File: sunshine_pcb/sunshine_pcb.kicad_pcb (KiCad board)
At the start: 4 copper layers, 42 x 52 mm, 54 parts, among them J1 Soldered, J2 Conn_01x03, J3 Soldered, J5 VerticalUSB, Q1 AO3400A, SW1 Fingertech, U1 ESP32-S3-WROOM-1, U2 SPX1117M3, U3 LIS3MDL, U4 ADXL375, U8 USBLC6-2P6

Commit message: Update PCB
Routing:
- added copper zone on In1.Cu, net /BATT1_+
- added copper zone on In2.Cu, net GND
- added copper zone on In1.Cu, net VDC
- removed copper zone on In2.Cu, net /BATT1_+
- removed copper zone on In1.Cu, net GND
- removed copper zone on In2.Cu, net VDC
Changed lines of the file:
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@@
 	)
 	(segment
+		(start 104.5 118.25)
+		(end 103 116.75)
+		(width 0.25)
+		(layer "F.Cu")
+		(net 20)
+	)
+	(segment
+		(start 103 116.75)
+		(end 102.41 116.75)
+		(width 0.25)
+		(layer "F.Cu")
+		(net 20)
+	)
+	(segment
 		(start 96.224 114.538588)
 		(end 98.511412 116.826)
@@
 	)
 	(segment
+		(start 103.468784 116.75)
+		(end 104.073 116.145784)
+		(width 0.25)
+		(layer "B.Cu")
+		(net 20)
+	)
+	(segment
 		(start 112.151 107.349)
 		(end 113.5 106)
@@
 	)
 	(segment
-		(start 102.425 116.75)
-		(end 103.222711 116.75)
-		(width 0.25)
-		(layer "B.Cu")
-		(net 20)
-	)
-	(segment
 		(start 96 133)
 		(end 96 131.1)
@@
 	)
 	(segment
-		(start 102.425 116.75)
-		(end 102.41 116.75)
-		(width 0.25)
-		(layer "B.Cu")
-		(net 20)
-	)
-	(segment
 		(start 96 109)
 		(end 96.75 109.75)
@@
 	)
 	(segment
-		(start 104.073 115.899711)
-		(end 104.073 115.637912)
-		(width 0.25)
-		(layer "B.Cu")
-		(net 20)
-	)
-	(segment
 		(start 107 115.5)
 		(end 108 115.5)
@@
 	)
 	(segment
-		(start 103.222711 116.75)
-		(end 104.073 115.899711)
-		(width 0.25)
-		(layer "B.Cu")
-		(net 20)
-	)
-	(segment
 		(start 108.75 115.5)
 		(end 112.589561 115.5)
@@
 	)
 	(segment
+		(start 102.41 116.75)
+		(end 103.468784 116.75)
+		(width 0.25)
+		(layer "B.Cu")
+		(net 20)
+	)
+	(segment
 		(start 99.613708 133.428)
 		(end 102.786293 133.428)
@@
 	)
 	(segment
+		(start 104.073 116.145784)
+		(end 104.073 115.637912)
+		(width 0.25)
+		(layer "B.Cu")
+		(net 20)
+	)
+	(segment
 		(start 103.25 110.75)
 		(end 102.5 110)
@@
 	)
 	(segment
-		(start 104.5 118.25)
-		(end 103.91 118.25)
-		(width 0.25)
-		(layer "In2.Cu")
-		(net 20)
-	)
-	(segment
-		(start 103.91 118.25)
-		(end 102.41 116.75)
-		(width 0.25)
-		(layer "In2.Cu")
-		(net 20)
-	)
-	(segment
 		(start 106 115.5)
 		(end 106.5 116)
@@
 	)
 	(segment
-		(start 102.454422 105.765833)
-		(end 103.970255 104.25)
-		(width 0.25)
-		(layer "In2.Cu")
-		(net 28)
-	)
-	(segment
-		(start 101.885412 105.674)
-		(end 102.362588 105.674)
+		(start 102.376026 105.65)
+		(end 100.823973 105.65)
 		(width 0.25)
-		(layer "In2.Cu")
+		(layer "In1.Cu")
 		(net 28)
 	)
 	(segment
-		(start 102.362588 105.674)
-		(end 102.454422 105.765833)
+		(start 104.25 104.25)
+		(end 103.776026 104.25)
 		(width 0.25)
-		(layer "In2.Cu")
+		(layer "In1.Cu")
 		(net 28)
 	)
 	(segment
-		(start 100.204559 106.269414)
+		(start 100.823973 105.65)
 		(end 98.602572 107.871401)
 		(width 0.25)
-		(layer "In2.Cu")
-		(net 28)
-	)
-	(segment
-		(start 103.970255 104.25)
-		(end 104.25 104.25)
-		(width 0.25)
-		(layer "In2.Cu")
-		(net 28)
-	)
-	(segment
-		(start 101.548 106.011412)
-		(end 101.885412 105.674)
-		(width 0.25)
-		(layer "In2.Cu")
-		(net 28)
-	)
-	(segment
-		(start 101.548 106.269414)
-		(end 100.204559 106.269414)
-		(width 0.25)
-		(layer "In2.Cu")
+		(layer "In1.Cu")
 		(net 28)
 	)
 	(segment
-		(start 101.548 106.269414)
-		(end 101.548 106.011412)
+		(start 103.776026 104.25)
+		(end 102.376026 105.65)
 		(width 0.25)
-		(layer "In2.Cu")
+		(layer "In1.Cu")
 		(net 28)
 	)
@@
 	)
 	(segment
-		(start 104.474 116.276)
-		(end 102.5 118.25)
+		(start 105.002983 108.758949)
+		(end 104.474 109.287932)
 		(width 0.15)
 		(layer "B.Cu")
@@
 	)
 	(segment
-		(start 102.5 118.25)
+		(start 103 118.25)
 		(end 96.17 118.25)
 		(width 0.15)
@@
 	)
 	(segment
-		(start 105.002983 108.758949)
-		(end 104.474 109.287932)
+		(start 104.474 109.287932)
+		(end 104.474 116.776)
 		(width 0.15)
 		(layer "B.Cu")
@@
 	)
 	(segment
-		(start 104.474 109.287932)
-		(end 104.474 116.276)
+		(start 104.474 116.776)
+		(end 103 118.25)
 		(width 0.15)
 		(layer "B.Cu")
@@
 	)
 	(segment
-		(start 103 115.5)
-		(end 103 118.25)
+		(start 103 116.1829)
+		(end 104.4571 117.64)
 		(width 0.15)
 		(layer "F.Cu")
@@
 	)
 	(segment
-		(start 103 118.25)
+		(start 104.72 117.64)
+		(end 105.18 118.1)
+		(width 0.15)
+		(layer "F.Cu")
+		(net 63)
+	)
+	(segment
+		(start 104.4571 117.64)
+		(end 104.72 117.64)
+		(width 0.15)
+		(layer "F.Cu")
+		(net 63)
+	)
+	(segment
+		(start 105.18 118.1)
+		(end 105.18 120.43)
+		(width 0.15)
+		(layer "F.Cu")
+		(net 63)
+	)
+	(segment
+		(start 105.18 120.43)
 		(end 107.6 122.85)
 		(width 0.15)
@@
 	)
 	(segment
+		(start 103 115.5)
+		(end 103 116.1829)
+		(width 0.15)
+		(layer "F.Cu")
+		(net 63)
+	)
+	(segment
 		(start 107.6 122.85)
 		(end 107.6 128.25)
@@
 	)
 	(zone
-		(net 18)
-		(net_name "GND")
+		(net 17)
+		(net_name "VDC")
 		(layer "In1.Cu")
 		(hatch edge 0.5)
+		(priority 4)
 		(connect_pads yes
 			(clearance 0.25)
@@
 		(polygon
 			(pts
-				(xy 118.5 139.1) (xy 83.4 139.1) (xy 77.6 103.3) (xy 77.8 86.3) (xy 86.1 84.9) (xy 119.3 85) (xy 123.5 88.3)
+				(xy 106.3 98) (xy 106.3 103) (xy 92.25 103.25) (xy 78.25 103.25) (xy 78.25 141) (xy 118.5 140.5)
+				(xy 133 99.5) (xy 120.8 98.1)
 			)
 		)
 	)
 	(zone
-		(net 17)
-		(net_name "VDC")
-		(layer "In2.Cu")
+		(net 64)
+		(net_name "/BATT1_+")
+		(layer "In1.Cu")
 		(hatch edge 0.5)
-		(priority 4)
+		(priority 1)
 		(connect_pads yes
 			(clearance 0.25)
@@
 		(polygon
 			(pts
-				(xy 106.3 98) (xy 106.3 103) (xy 92.25 103.25) (xy 78.25 103.25) (xy 78.25 141) (xy 118.5 140.5)
-				(xy 133 99.5) (xy 120.8 98.1)
+				(xy 99.3 96.6) (xy 106.3 98) (xy 120.8 98.1) (xy 120.8 92.9) (xy 107 86.7) (xy 99.1 86.6)
 			)
 		)
 	)
 	(zone
-		(net 64)
-		(net_name "/BATT1_+")
+		(net 18)
+		(net_name "GND")
 		(layer "In2.Cu")
 		(hatch edge 0.5)
-		(priority 1)
 		(connect_pads yes
 			(clearance 0.25)
@@
 		(polygon
 			(pts
-				(xy 99.3 96.6) (xy 106.3 98) (xy 120.8 98.1) (xy 120.8 92.9) (xy 107 86.7) (xy 99.1 86.6)
+				(xy 118.5 139.1) (xy 83.4 139.1) (xy 77.6 103.3) (xy 77.8 86.3) (xy 86.1 84.9) (xy 119.3 85) (xy 123.5 88.3)
 			)
 		)

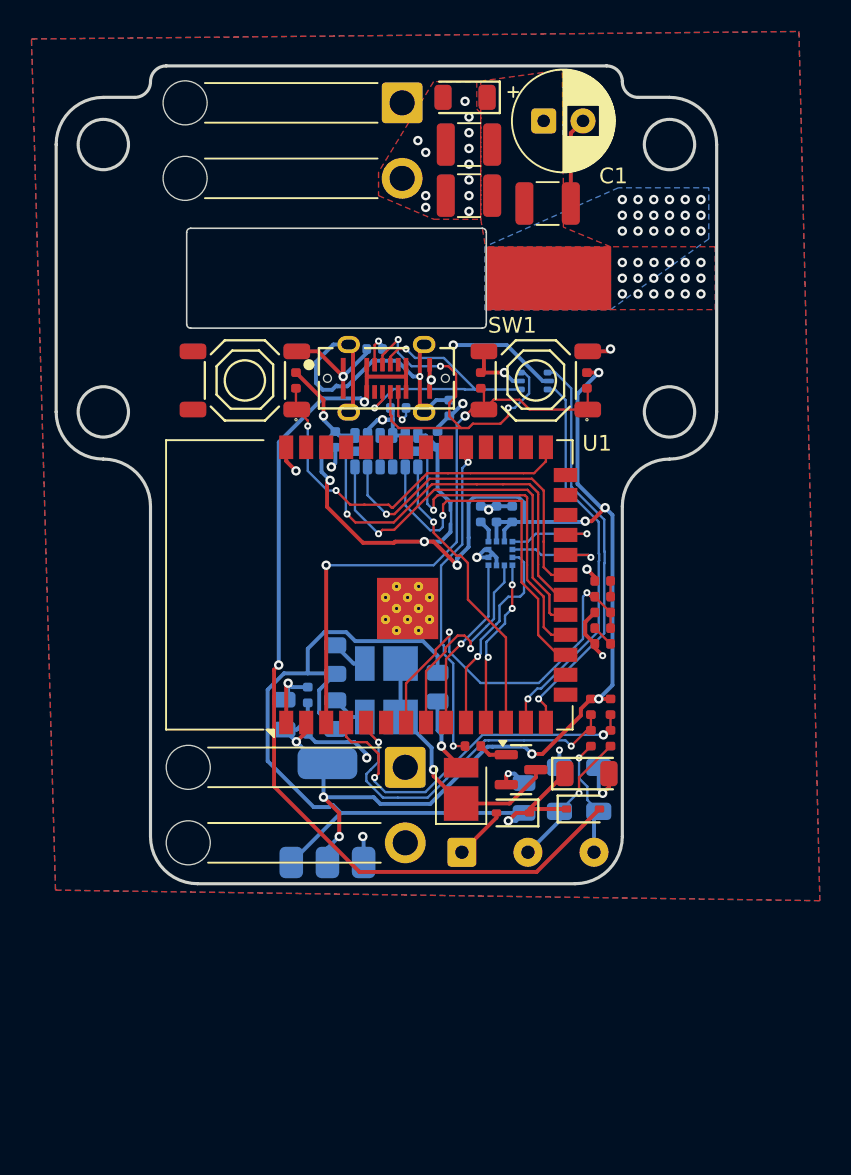
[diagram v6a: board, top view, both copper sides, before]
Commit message: Re-design PCB to not interact with VDC
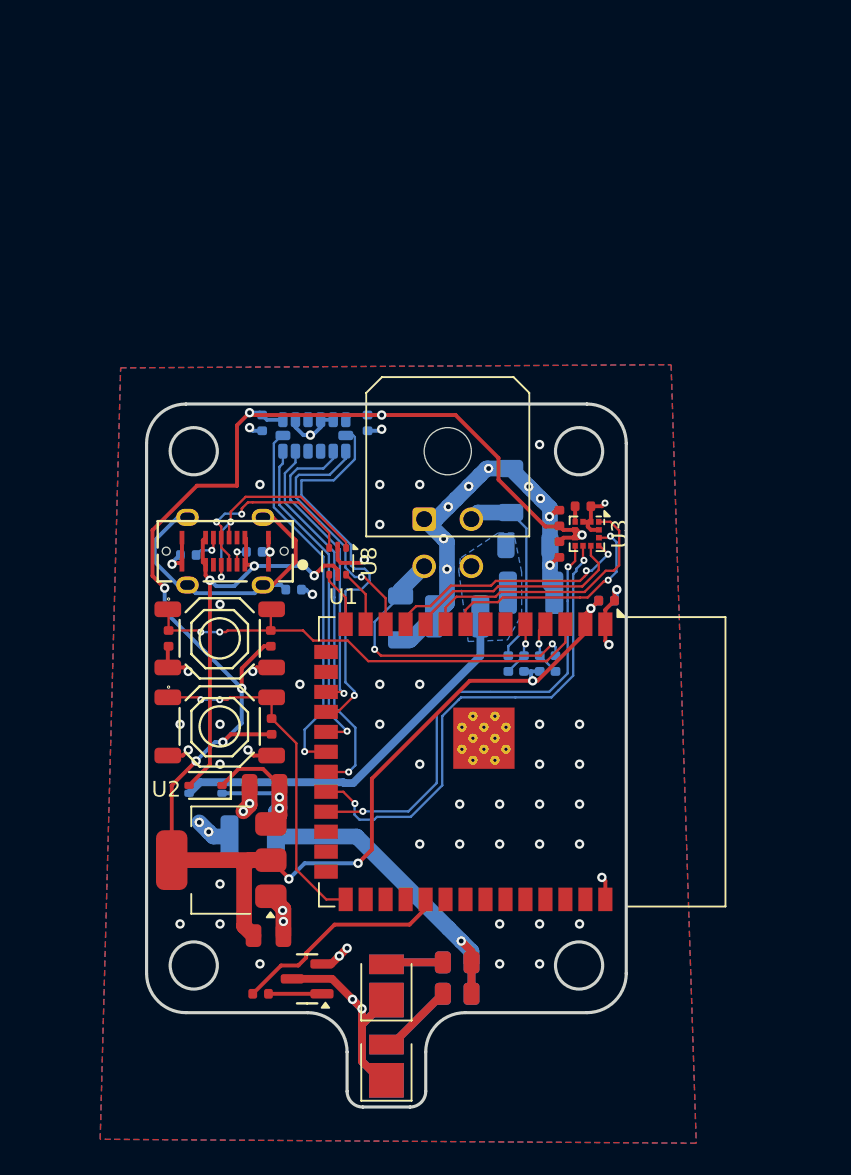
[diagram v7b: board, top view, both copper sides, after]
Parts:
- removed C1: 220u, Capacitor_THT:CP_Radial_D6.3mm_P2.50mm
- removed C30: 100nF, PCM_JLCPCB:C_0402
- removed D7: SMF12A, PCM_JLCPCB:D_SOD-123FL
- removed J1, J3: Soldered, Connector_Wire:SolderWire-0.75sqmm_1x02_P4.8mm_D1.25mm_OD2.3mm_Relief
- removed R15, R16, R17: 5.1kΩ, PCM_JLCPCB:R_0402
- removed R18: 1kΩ, PCM_JLCPCB:R_0402
- removed SW1: Fingertech, custom:FingertechSwitch
- added D6: LED, LED_SMD:LED_PLCC_2835, B.Cu at (100.0, 150.1)
- added R8: 33Ω, PCM_JLCPCB:R_0805, B.Cu at (104.5, 145.5)
- C2, C3, C4, D2, D5, D8, R20, R21, R6, R7: moved to B.Cu
- C27, C28, C29, C5, C6, C9, D1, D4, R10, R12, U2, U3, U8: moved to F.Cu
- J2: value Conn_01x03 -> Conn_01x04; footprint Connector_Wire:SolderWire-0.25sqmm_1x03_P4.2mm_D0.65mm_OD1.7mm -> Connector_Molex:Molex_Micro-Fit_3.0_43045-0400_2x02_P3.00mm_Horizontal
- moved C4 43.0 mm to (91.5, 135.5)
- moved C2 28.8 mm to (109.2, 120.0), turned to 0 degrees
- moved C3 26.9 mm to (104.5, 121.5), turned to 180 degrees
- moved R4 25.9 mm to (92.7, 122.9), turned to 90 degrees
- moved S1 25.9 mm to (89.4, 122.9), turned to 0 degrees
- moved C7 25.7 mm to (86.2, 122.9), turned to -90 degrees
- moved D3 24.0 mm to (88.5, 132.2), turned to 180 degrees
- moved D4 22.2 mm to (100.0, 150.1), turned to 90 degrees
- moved S2 22.1 mm to (89.4, 128.5), turned to 0 degrees
- moved R5 22.1 mm to (92.7, 128.5), turned to 90 degrees
- moved J2 21.3 mm to (102.4, 115.3)
- moved R10 20.8 mm to (104.5, 143.5), turned to 180 degrees
- moved R11 20.7 mm to (92.0, 145.5)
- moved C9 20.6 mm to (114.0, 120.5), turned to 0 degrees
- moved D1 20.5 mm to (100.0, 145.0), turned to 90 degrees
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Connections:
- C2 pad 1: VDC -> /5V_IN
- C3 pad 1: VDC -> /5V_IN
- C4 pad 1: VDC -> +5V
- D8 pad 1: +5V -> /5V_IN
- J2 pad 1: /5V_IN -> GND
- J2 pad 2: /S1_C -> /S2_C
- J2 pad 3: /S2_C -> /S1_C
- S2 pad 2: unconnected-(S2-B-Pad2) -> /BOOT
- S2 pad 4: unconnected-(S2-D-Pad4) -> GND
- U1 pad 7: /VBUS_DIV -> unconnected-(U1-IO7-Pad7)
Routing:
- net VBUS: track 74.2 -> 29.2 mm
- net /MAG_DRDY: track 6.87 -> 31.8 mm, vias 1 -> 2
- net /VBUS_DIV: track 24.7 -> 0.00 mm, vias 2 -> 0
- net /MAG_INT: track 6.34 -> 29.9 mm, vias 1 -> 2
- net /USB_D+: track 26.0 -> 3.58 mm, vias 1 -> 0
- net /5V_IN: track 3.41 -> 24.7 mm
- net /USB_D-: track 24.9 -> 3.66 mm, vias 1 -> 0
- net +5V: track 56.5 -> 35.3 mm, vias 1 -> 3
- net /S1: track 23.2 -> 3.60 mm, vias 2 -> 1
- net /S2: track 22.2 -> 3.46 mm, vias 2 -> 1
- net +3V3: track 110.4 -> 123.6 mm, vias 12 -> 11
- net /USB_C_D+: track 24.7 -> 12.7 mm, vias 3 -> 2
- net /S1_C: track 8.98 -> 19.2 mm, vias 1 -> 2
- net GND: track 59.3 -> 69.4 mm, vias 29 -> 68
- net /EN: track 38.4 -> 30.6 mm
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- added copper zone on B.Cu, net /5V_IN
- added copper zone on In1.Cu, net GND
- removed copper zone on B.Cu, net /BATT1_+
- removed copper zone on In1.Cu, net /BATT1_+
- removed copper zone on F.Cu, net VDC
- removed copper zone on In1.Cu, net VDC
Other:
- board size 42 x 52 mm -> 30.5 x 44.7 mm

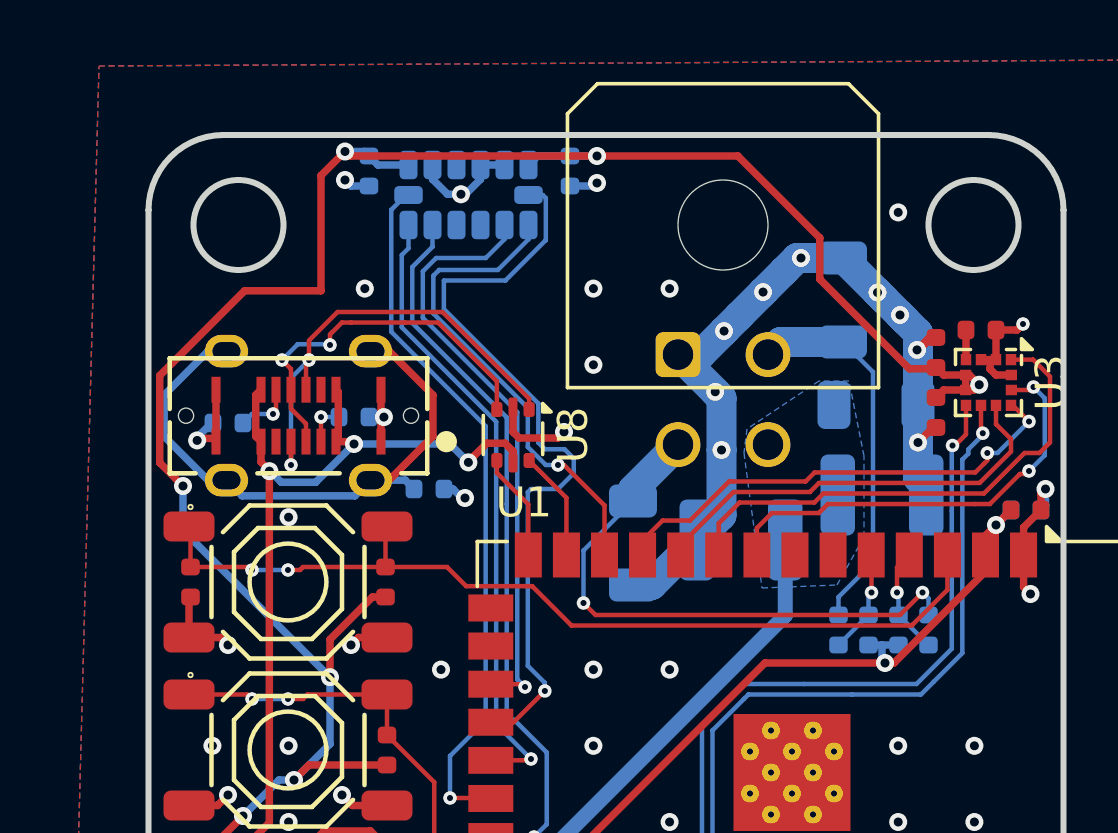
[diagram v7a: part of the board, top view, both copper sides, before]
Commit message: Change connector to be soldered
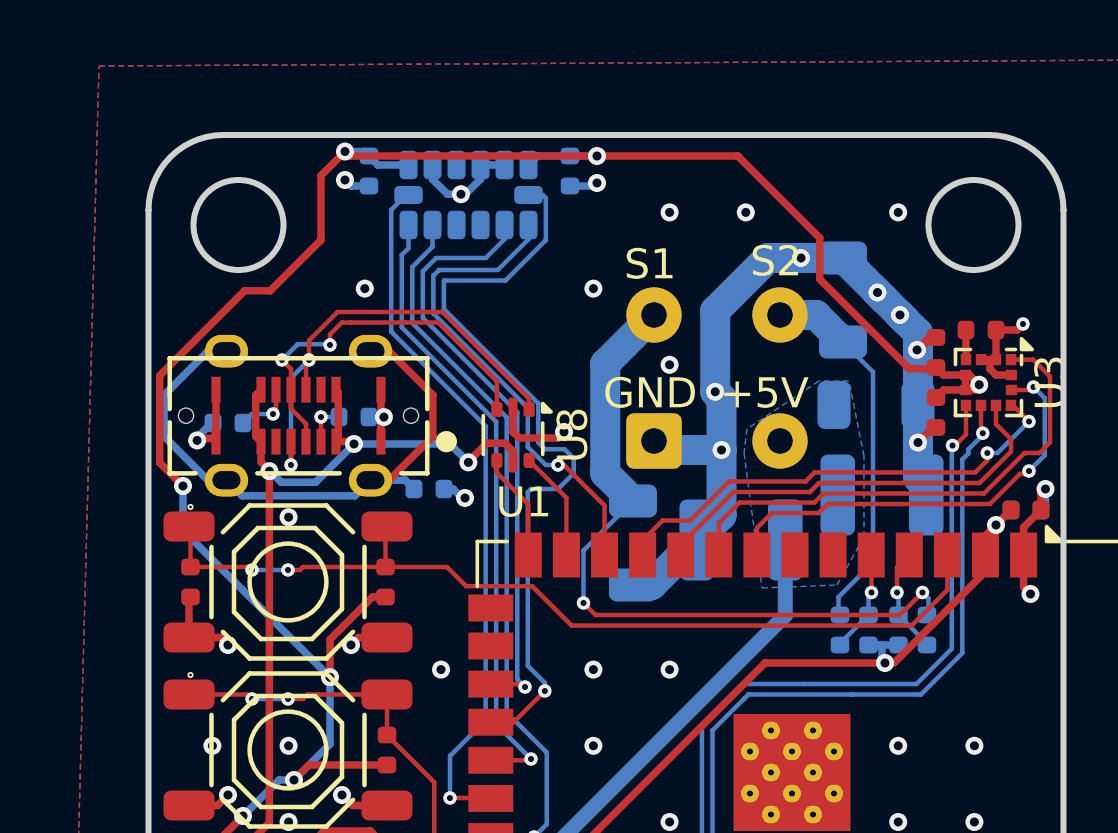
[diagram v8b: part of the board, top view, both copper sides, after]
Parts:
- J2: footprint Connector_Molex:Molex_Micro-Fit_3.0_43045-0400_2x02_P3.00mm_Horizontal -> custom:SolderConnector4P
- moved J2 2.99 mm to (101.6, 118.2)
- moved R20 2.95 mm to (107.8, 124.5)
- moved R21 2.95 mm to (110.7, 124.5)
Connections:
- J2 pad 2: /S2_C -> /S1_C
- J2 pad 3: /S1_C -> /S2_C
- R20 pad 1: /S1 -> /S2
- R20 pad 2: /S1_C -> /S2_C
- R21 pad 1: /S2 -> /S1
- R21 pad 2: /S2_C -> /S1_C
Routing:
- net /S1_C: track 19.2 -> 23.9 mm
- net GND: track 69.4 -> 70.8 mm, vias 68 -> 67
- net +3V3: track 123.6 -> 122.6 mm
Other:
- board text added: "+5V"
- board text added: "GND"
- board text added: "S1"
- board text added: "S2"
